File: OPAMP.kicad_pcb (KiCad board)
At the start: 2 copper layers, 49 parts, among them J1 GH125-S02CCA-00, J2 GH125-S06DCA-00, J3 GH125-S03DCA-00, SW1 DSHP02TSGET, U1 ADG704BRMZ-REEL, U2 AD8421BRZ-RL, U3 OPA2197QDGKRQ1, U4 REF2030AIDDCR

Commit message: Layout
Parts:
- C11: value 1uF -> 4.7uF
- C12: value 330pF -> 47nF
- R11, R12: value 1M -> 100K; moved to B.Cu
- R14: value 330K -> 68K
- R15: value 4.99K -> 1K
- R18: value 143K -> 28.7K
- R3, R4: value 100 -> 0
- moved C10 141.7 mm to (60.6, 127.9)
- moved FB1 139.0 mm to (61.0, 129.1)
- moved C8 136.8 mm to (63.5, 129.4)
- moved C7 134.3 mm to (63.5, 128.6)
- moved C9 131.9 mm to (60.6, 127.0)
- moved R11 115.7 mm to (64.1, 137.2)
- moved C11 113.6 mm to (69.3, 136.8)
- moved R12 113.4 mm to (64.1, 136.3)
- moved R15 113.2 mm to (71.9, 130.4)
- moved R18 111.9 mm to (69.3, 132.6), turned to -90 degrees
- moved R19 109.5 mm to (71.0, 132.6), turned to -90 degrees
- moved R14 108.9 mm to (69.3, 137.6), turned to 180 degrees
- moved C12 107.9 mm to (70.2, 132.6), turned to -90 degrees
- moved C14 104.0 mm to (71.9, 132.6), turned to 90 degrees
- moved J3 64.0 mm to (75.7, 135.0), turned to 90 degrees
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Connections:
- net /COIL_N_FILT renamed /COIL_FILT_N
- net /COIL_N_RAW renamed /COIL_RAW_N
- net /COIL_P_FILT renamed /COIL_FILT_P
- net /COIL_P_RAW renamed /COIL_RAW_P
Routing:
- net /AGND_SHIELD: track 0.00 -> 67.5 mm
- net +5VA: track 0.00 -> 39.0 mm, vias 0 -> 2
- net /BIAS_1V5: track 0.00 -> 27.5 mm, vias 0 -> 3
- net Net-(U1-EN): track 0.00 -> 14.2 mm, vias 0 -> 2
- net Net-(U1-A0): track 0.00 -> 13.0 mm, vias 0 -> 2
- net /HP_IN: track 0.00 -> 12.5 mm
- net Net-(U1-A1): track 0.00 -> 12.0 mm, vias 0 -> 2
- net /+5VIN: track 0.00 -> 11.7 mm
- net /COIL_FILT_N: track 0.00 -> 11.4 mm, vias 0 -> 3
- net /COIL_FILT_P: track 0.00 -> 11.0 mm, vias 0 -> 1
- net /VOUT_RAW: track 0.00 -> 10.7 mm, vias 0 -> 2
- net /RG_A: track 0.00 -> 10.7 mm
- net /BIAS_FILT: track 0.00 -> 9.66 mm
- net /RG_B: track 0.00 -> 8.83 mm
- net /VOUT: track 0.00 -> 7.80 mm, vias 0 -> 2
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- added copper zone on F.Cu, net +5VA
- added copper zone on F.Cu, net /+5VIN
- added copper zone on B.Cu, net /AGND
- added copper zone on F.Cu, net /AGND
- added copper zone on F.Cu, net /BIAS_FILT
- added copper zone on F.Cu, net /COIL_FILT_N
- added copper zone on F.Cu, net /COIL_FILT_P
- added copper zone on F.Cu, net /RG_A
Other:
- board outline added: 33 x 23 mm

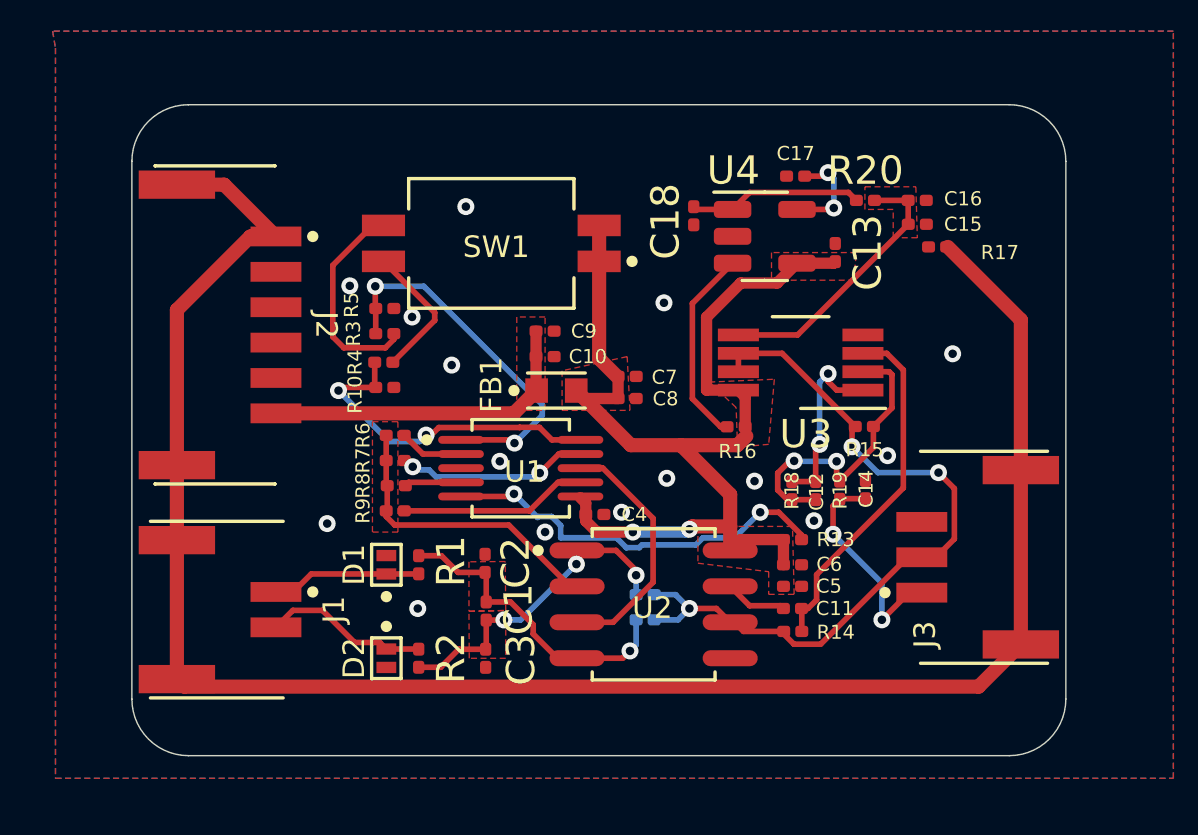
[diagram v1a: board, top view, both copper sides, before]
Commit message: 更换蛇形走线
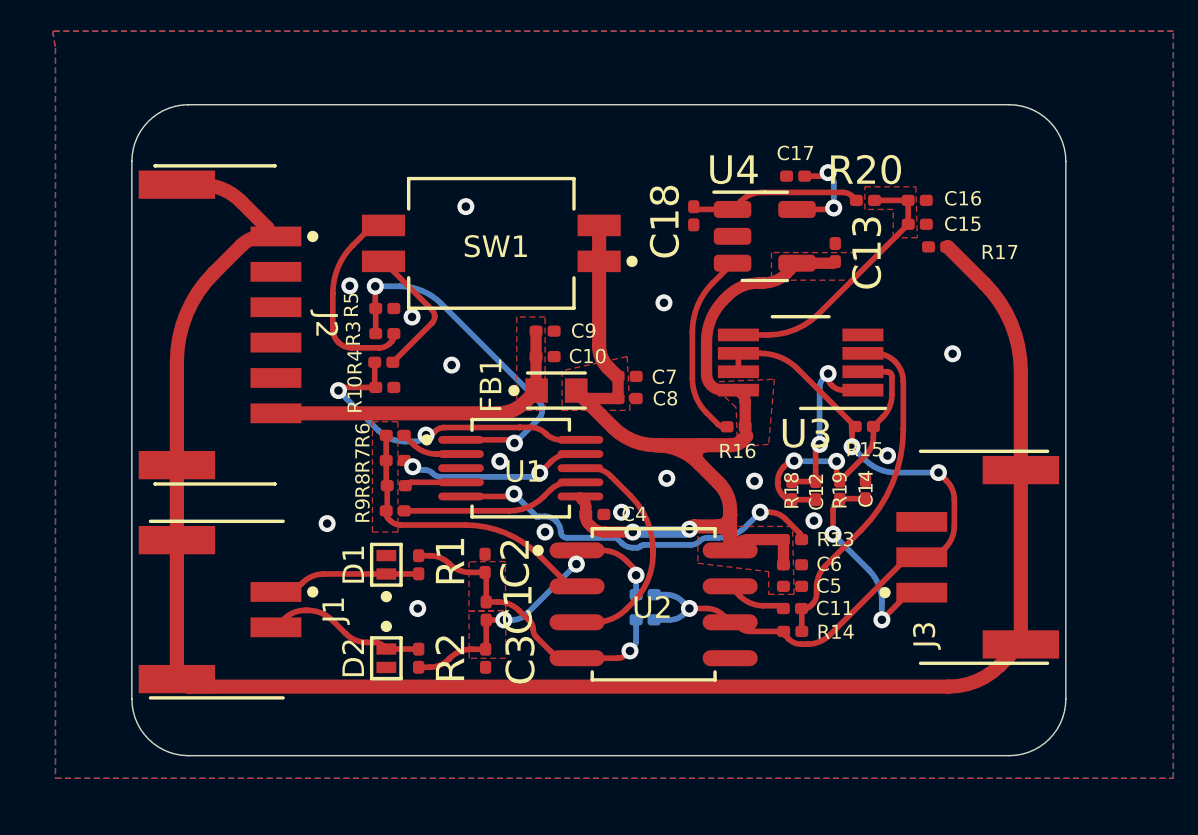
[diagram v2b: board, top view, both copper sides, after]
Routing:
- net /AGND_SHIELD: track 67.5 -> 66.3 mm
- net +5VA: track 39.0 -> 40.1 mm

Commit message: update
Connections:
- D1 pad 2: /AGND -> /AGND_SHIELD
- D2 pad 2: /AGND -> /AGND_SHIELD
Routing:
- net /COIL_FILT_P: vias 1 -> 3
- added copper zone on F.Cu, net /AGND_SHIELD
